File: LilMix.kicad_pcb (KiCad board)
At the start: 2 copper layers, 73.2 x 62.3 mm, 59 parts, among them J1 Conn_01x03, J1_L1 MONO, J1_R1 MONO, J2_L1 MONO, J2_R1 MONO, J3 STEREO, J4 MONO, J5 MONO, J6 STEREO, J7 MONO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

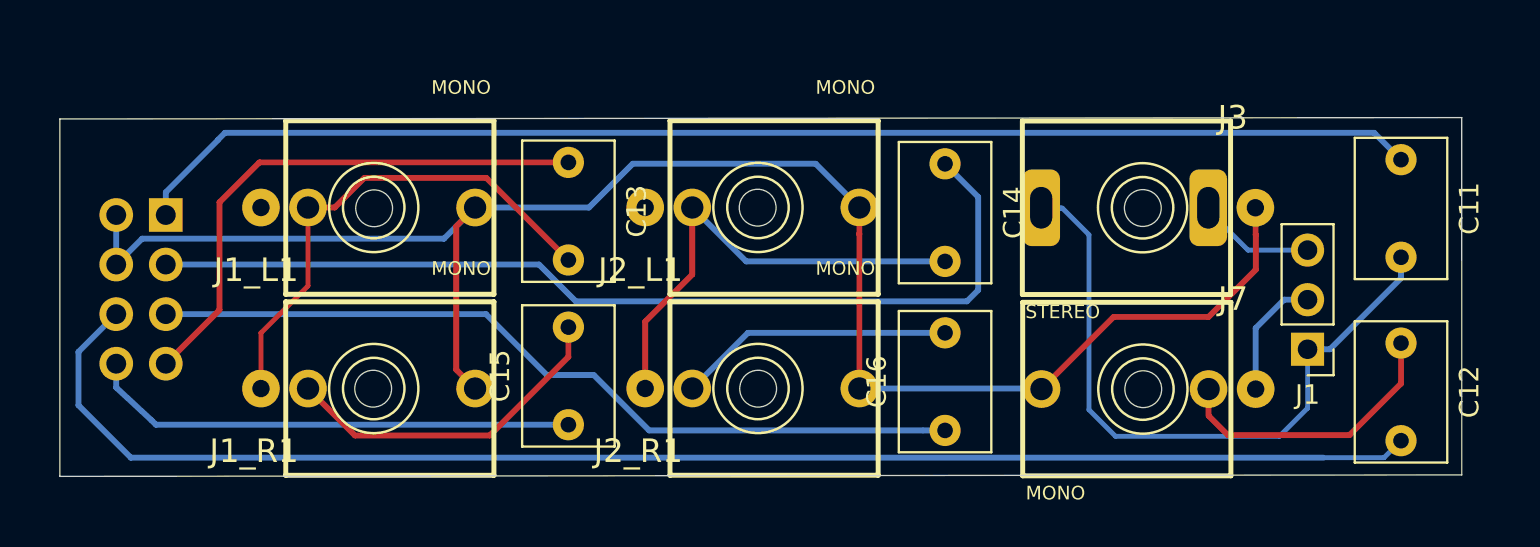
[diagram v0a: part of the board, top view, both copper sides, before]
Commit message: Reduced top board width.
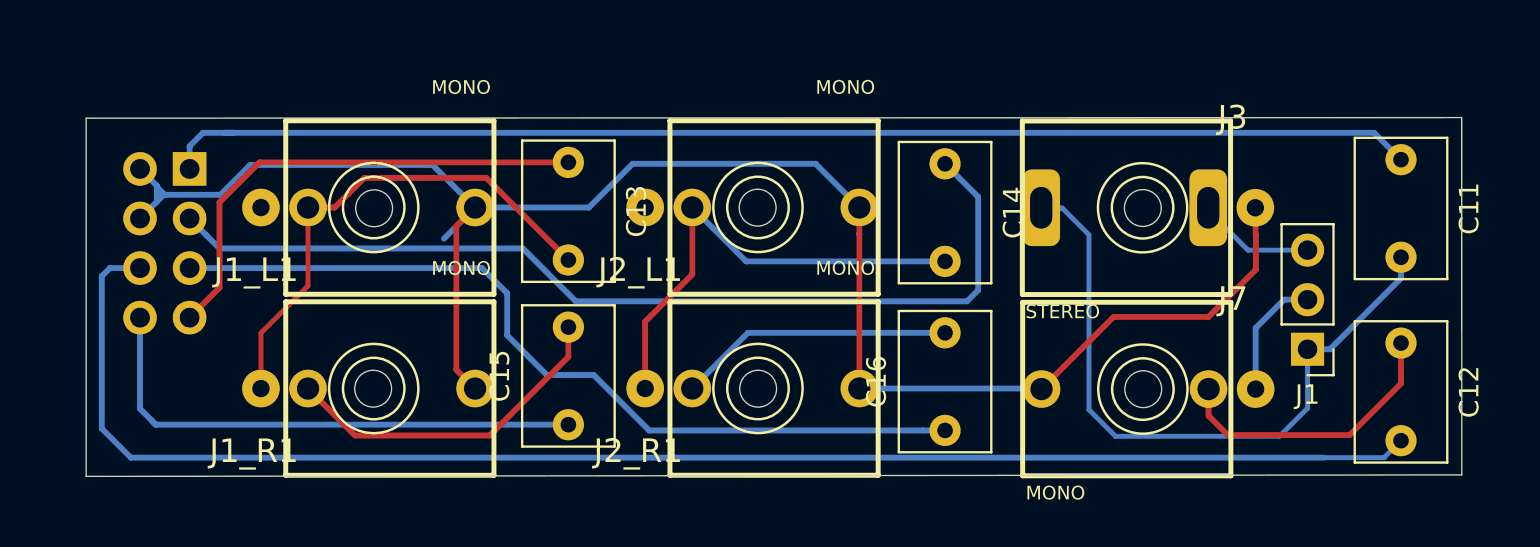
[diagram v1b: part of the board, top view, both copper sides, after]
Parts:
- moved JP2 2.66 mm to (92.4, 121.2)
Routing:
- net J1_R_B: track 25.1 -> 28.1 mm
- net J1_L_B: track 28.1 -> 25.3 mm
- net J3_R_B: track 74.7 -> 77.5 mm
- net GND_B: track 89.0 -> 91.4 mm
- net J3_L_B: track 66.3 -> 64.5 mm
- net J2_R_B: track 42.4 -> 43.4 mm
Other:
- outline, holes or cut-outs redrawn

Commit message: Change diode values
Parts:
- D1, D2: value 1N5819 -> 1N5818
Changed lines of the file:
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@@
   )
   (setup
-    (last_trace_width 0.3)
+    (last_trace_width 0.25)
     (user_trace_width 0.3)
     (user_trace_width 0.4)
@@
       (effects (font (size 1 1) (thickness 0.15)) (justify mirror))
     )
-    (fp_text value 1N5819 (at 0 -2.1) (layer B.Fab)
+    (fp_text value 1N5818 (at 0 -2.1) (layer B.Fab)
       (effects (font (size 1 1) (thickness 0.15)) (justify mirror))
     )
@@
       (effects (font (size 1 1) (thickness 0.15)) (justify mirror))
     )
-    (fp_text value 1N5819 (at 0 -2.1) (layer B.Fab)
-      (effects (font (size 1 1) (thickness 0.15)) (justify mirror))
-    )
+    (fp_text value 1N5818 (at 0 -2.1) (layer B.Fab)
+      (effects (font (size 1 1) (thickness 0.15)) (justify mirror))
+    )

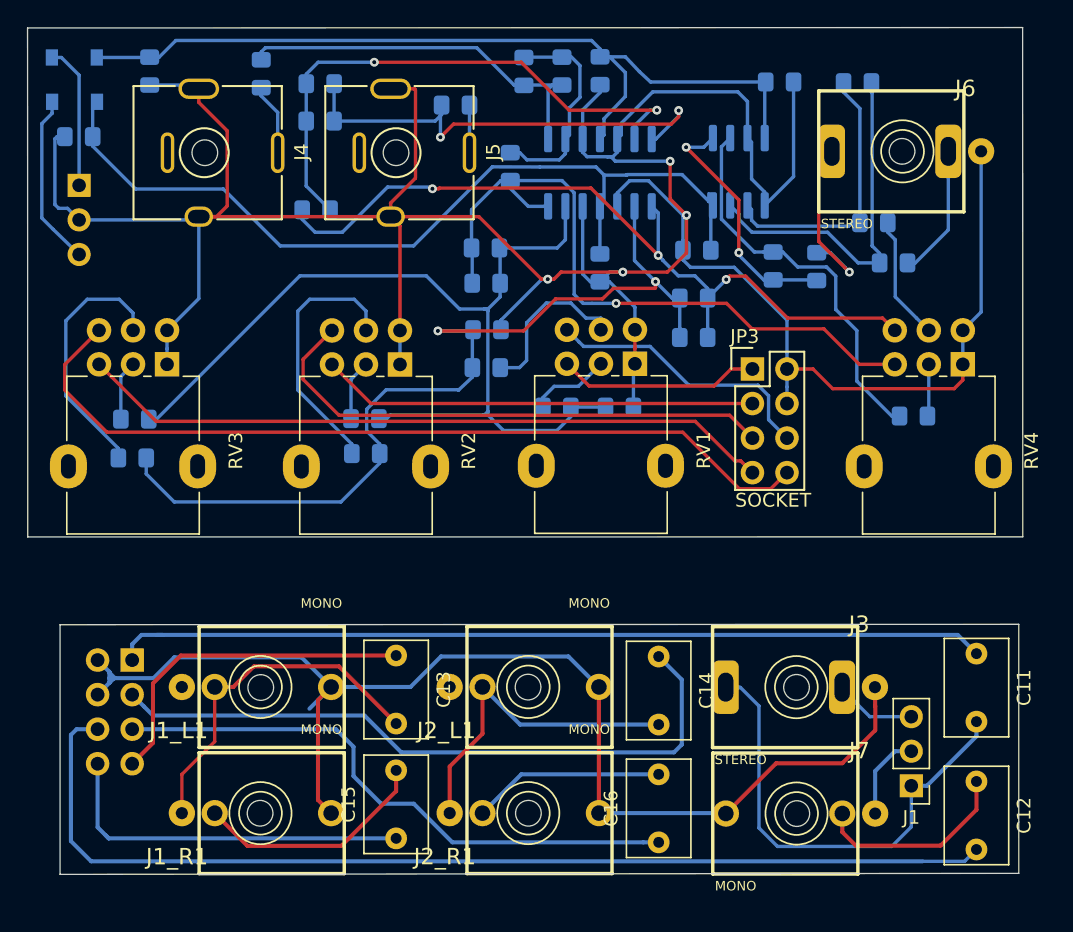
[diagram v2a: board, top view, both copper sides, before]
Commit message: Footprints changed and title text added
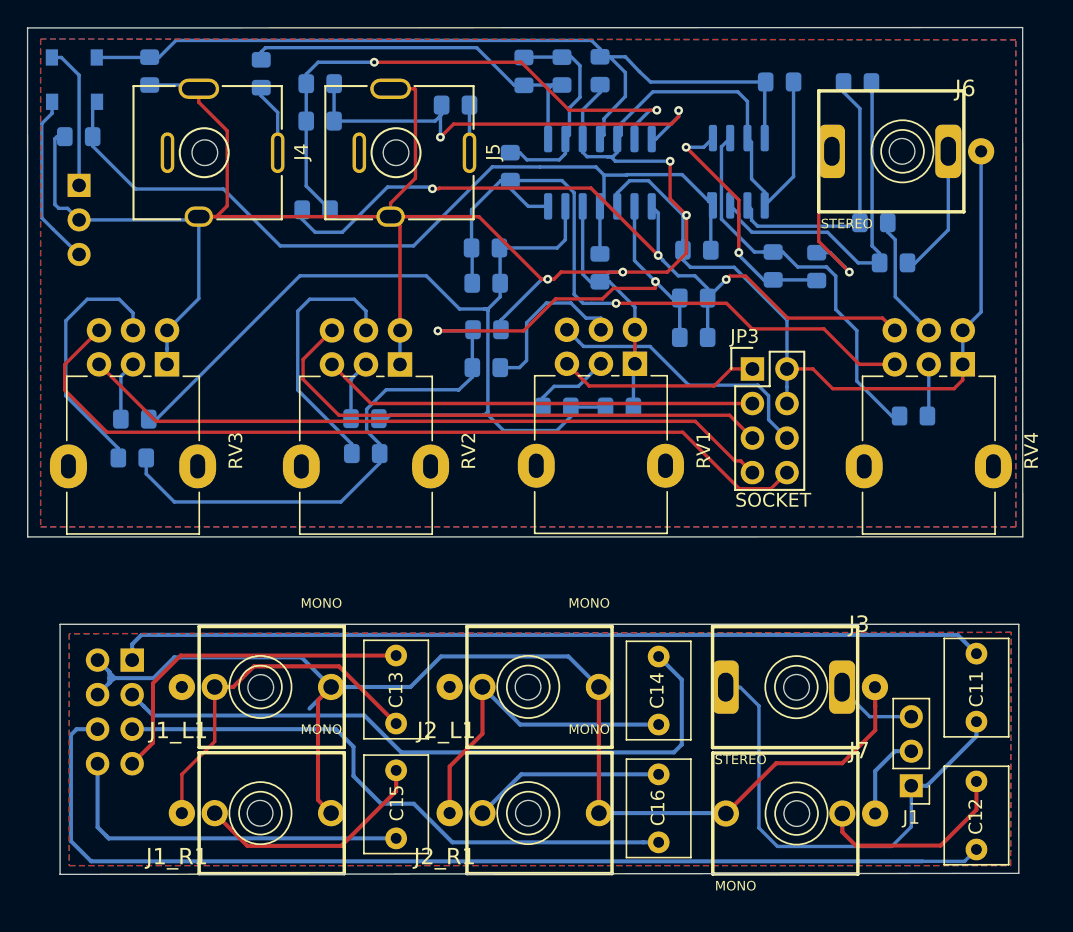
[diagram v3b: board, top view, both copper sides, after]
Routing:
- added copper zone on B.Cu, net GND
- added copper zone on F.Cu, net GND
- added copper zone on B.Cu, net GND_B
- added copper zone on F.Cu, net GND_B
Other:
- board text added: "CopyCat Modules"
- board text added: "LILMIX"
- board text added: "cc-by-sa"
- board text added: "r001"
- board text added: "rear"

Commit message: Fixed fp on mono jacks.
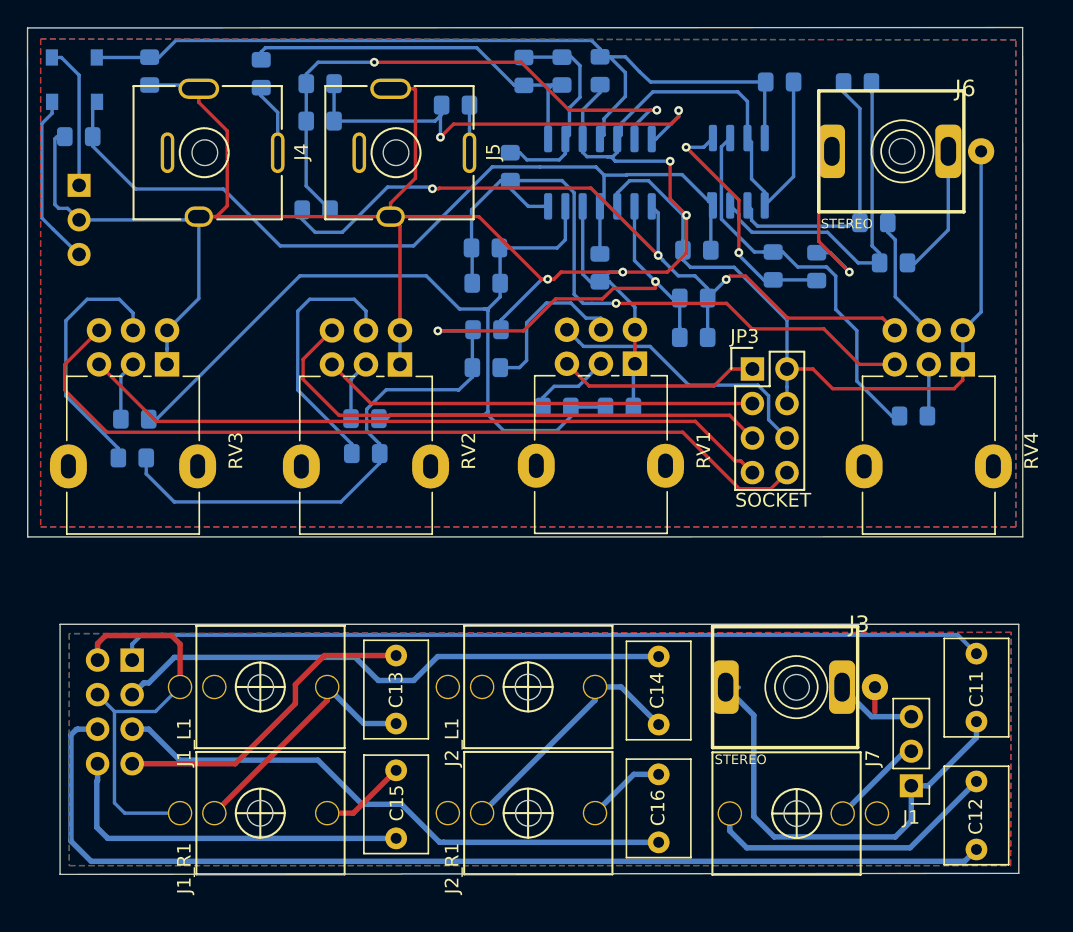
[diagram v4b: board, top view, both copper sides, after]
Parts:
- J1_L1, J1_R1, J2_L1, J2_R1, J7: footprint 4ms-footprints:PJ301M-12 -> Eurocad:PJ301M-12-CC-TIGHT
- turned J1_L1 to 270 degrees
- turned J1_R1 to 270 degrees
- turned J2_L1 to 270 degrees
- turned J2_R1 to 270 degrees
- turned J7 to 90 degrees
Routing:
- net J3_R_B: track 77.5 -> 141.7 mm
- net GND_B: track 91.4 -> 32.2 mm
- net J1_R_B: track 28.1 -> 50.6 mm
- net Net-(C15-Pad2): track 17.5 -> 6.37 mm
- net J2_L_B: track 49.6 -> 41.3 mm
- net Net-(C16-Pad2): track 14.1 -> 5.86 mm
- net Net-(C12-Pad1): track 14.8 -> 22.0 mm
- net J1_INSERT: track 26.0 -> 18.9 mm
- net J2_INSERT: track 24.4 -> 18.5 mm
- net J1_L_B: track 25.3 -> 23.5 mm
- net J2_R_B: track 43.4 -> 42.2 mm
- net J3_R_INSERT: track 5.84 -> 6.59 mm
- net J3_L_INSERT: track 35.7 -> 35.1 mm
- net Net-(J1-Pad2): track 6.39 -> 6.94 mm
